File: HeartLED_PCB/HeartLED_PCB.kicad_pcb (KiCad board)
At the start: 2 copper layers, 58.8 x 52.2 mm, 37 parts, among them U1 ICM7555IBAZ-T, U2 CD4017BM96, U3 TPS61222DCKR, U4 HX SS12F44G4

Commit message: Routing done
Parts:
- removed BT1: Battery_Cell, Battery:BatteryHolder_Keystone_1060_1x2032
- removed C2, C3: 10uF, FOOTPRINTS:CL10A106MQ8NNNC
- removed the G*** at (123.5, 81.7)
- removed L1: 4.7uH, FOOTPRINTS:LQH3NPN4R7MMEL
- removed TP1, TP2, TP3: TestPoint, TestPoint:TestPoint_Pad_D1.0mm
- removed U3: TPS61222DCKR, FOOTPRINTS:TPS61222DCKR
- removed U4: HX SS12F44G4, FOOTPRINTS:HX SS12F44G4
- added G***: LOGO, FOOTPRINTS:raccoon, F.Cu at (128.5, 108.1)
- added SW1: SS12D00G3, FOOTPRINTS:SS12D00G3, F.Cu at (148.8, 93.9)
- C1: value 4.7uF -> 47uF; footprint FOOTPRINTS:CL10A475KP8NNNC -> Capacitor_THT:C_Radial_D5.0mm_H7.0mm_P2.00mm; moved to F.Cu
- H1: footprint MountingHole:MountingHole_2.1mm -> MountingHole:MountingHole_2.7mm
- R1: value 100k -> 1k; footprint FOOTPRINTS:0603WAJ0104T5E -> Resistor_THT:R_Axial_DIN0207_L6.3mm_D2.5mm_P7.62mm_Horizontal; moved to F.Cu
- R10, R3, R4, R5, R6, R7, R8, R9: value 3.3k -> 1k; footprint FOOTPRINTS:0402WGJ0332TCE -> Resistor_THT:R_Axial_DIN0207_L6.3mm_D2.5mm_P7.62mm_Horizontal
- R11: value 3.3k -> 10K; footprint FOOTPRINTS:0402WGJ0332TCE -> Resistor_THT:R_Axial_DIN0207_L6.3mm_D2.5mm_P7.62mm_Horizontal
- R12: value 3.3k -> 1OK; footprint FOOTPRINTS:0402WGJ0332TCE -> Resistor_THT:R_Axial_DIN0207_L6.3mm_D2.5mm_P7.62mm_Horizontal
- R2: value 10k -> 1k; footprint FOOTPRINTS:0402WGJ0103TCE -> Resistor_THT:R_Axial_DIN0207_L6.3mm_D2.5mm_P7.62mm_Horizontal; moved to F.Cu
- U1: value ICM7555IBAZ-T -> NE555DR; footprint FOOTPRINTS:ICM7555IBAZ-T -> FOOTPRINTS:NE555DR; moved to F.Cu
- U2: value CD4017BM96 -> 1066; footprint FOOTPRINTS:CD4017BM96 -> FOOTPRINTS:1066; moved to B.Cu
- moved R5 51.7 mm to (153.1, 102.0), turned to 180 degrees
- moved D4 51.3 mm to (156.8, 85.9), turned to 180 degrees
- moved D10 48.2 mm to (127.5, 121.4), turned to 0 degrees
- moved D6 46.9 mm to (113.8, 75.7)
- moved D7 42.5 mm to (102.2, 97.1), turned to 0 degrees
- moved R12 41.7 mm to (138.0, 116.4)
- moved R11 40.9 mm to (127.7, 116.4), turned to 180 degrees
- moved R4 39.8 mm to (150.4, 82.3)
- moved R8 35.5 mm to (140.0, 82.3)
- moved R2 34.9 mm to (106.9, 82.5)
- moved R1 29.8 mm to (124.9, 87.0)
- moved G*** 28.7 mm to (130.6, 112.3)
- moved D5 28.5 mm to (145.4, 108.5)
- moved R7 26.4 mm to (114.5, 87.0), turned to 180 degrees
- moved R9 26.3 mm to (142.8, 87.0), turned to 0 degrees
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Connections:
- C1 pad 1: Net-(U1-THRESHOLD) -> Net-(U1-THRES)
- D1 pad 2: Net-(D1-A) -> VCC
- D10 pad 1: Net-(D10-K) -> GND
- D2 pad 2: Net-(D2-A) -> VCC
- D3 pad 2: Net-(D3-A) -> VCC
- D4 pad 2: Net-(D4-A) -> VCC
- D5 pad 2: Net-(D5-A) -> VCC
- D6 pad 1: Net-(D6-K) -> GND
- D7 pad 1: Net-(D7-K) -> GND
- D8 pad 1: Net-(D8-K) -> GND
- D9 pad 1: Net-(D9-K) -> GND
- R1 pad 1: ASTABLE_OUTPUT -> Net-(D1-K)
- R1 pad 2: Net-(U1-THRESHOLD) -> Net-(U1-OUT)
- R10 pad 1: GND -> Net-(U1-OUT)
- R10 pad 2: Net-(D8-K) -> Net-(D10-A)
- R11 pad 1: GND -> Net-(U1-DISCH)
- R11 pad 2: Net-(D9-K) -> Net-(U1-THRES)
- R12 pad 1: GND -> VCC
- R12 pad 2: Net-(D10-K) -> Net-(U1-DISCH)
- R2 pad 1: Net-(U1-DISCHARGE) -> Net-(D2-K)
- R2 pad 2: +5V -> Net-(U1-OUT)
- R3 pad 1: Net-(D1-K) -> Net-(D3-K)
- R3 pad 2: GND -> Net-(U1-OUT)
- R4 pad 1: Net-(D2-K) -> Net-(D4-K)
- R4 pad 2: GND -> Net-(U1-OUT)
- R5 pad 1: Net-(D3-K) -> Net-(D5-K)
- R5 pad 2: GND -> Net-(U1-OUT)
- R6 pad 1: Net-(D4-K) -> Net-(U1-OUT)
- R6 pad 2: GND -> Net-(D6-A)
- R7 pad 1: GND -> Net-(U1-OUT)
- R7 pad 2: Net-(D5-K) -> Net-(D7-A)
- R8 pad 1: Net-(D6-K) -> Net-(U1-OUT)
- R8 pad 2: GND -> Net-(D8-A)
- R9 pad 1: Net-(D7-K) -> Net-(U1-OUT)
- R9 pad 2: GND -> Net-(D9-A)
- U1 pad 2: Net-(U1-THRESHOLD) -> Net-(U1-THRES)
- U1 pad 3: ASTABLE_OUTPUT -> Net-(U1-OUT)
- U1 pad 4: +5V -> VCC
- U1 pad 5: GND -> unconnected-(U1-CONT-Pad5)
- U1 pad 6: Net-(U1-THRESHOLD) -> Net-(U1-THRES)
- U1 pad 7: Net-(U1-DISCHARGE) -> Net-(U1-DISCH)
- U1 pad 8: +5V -> VCC
- U2 pad 1: Net-(D1-A) -> GND
- U2 pad 2: Net-(D2-A) -> Net-(SW1-Pad2)
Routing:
- net Net-(U1-OUT): track 0.00 -> 104.6 mm
- net +5V: track 69.5 -> 0.00 mm, vias 1 -> 0
- net +3V: track 49.1 -> 0.00 mm
- net Net-(U1-THRES): track 0.00 -> 38.9 mm
- net ASTABLE_OUTPUT: track 36.8 -> 0.00 mm, vias 1 -> 0
- net Net-(D3-A): track 27.3 -> 0.00 mm
- net Net-(D2-A): track 25.8 -> 0.00 mm
- net Net-(U1-THRESHOLD): track 25.1 -> 0.00 mm
- net Net-(U1-DISCH): track 0.00 -> 23.4 mm
- net Net-(BT1-+): track 20.2 -> 0.00 mm
- net Net-(D4-A): track 18.2 -> 0.00 mm
- net Net-(D9-A): track 29.0 -> 11.0 mm
- net Net-(SW1-Pad2): track 0.00 -> 16.9 mm
- net Net-(D5-A): track 12.3 -> 0.00 mm
- net Net-(D1-A): track 10.4 -> 0.00 mm
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- added copper zone on F.Cu, net VCC
- removed copper zone on F.Cu, net GND
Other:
- board size 58.8 x 52.2 mm -> 61.9 x 55.1 mm
- board text removed: "Happy Valentine's Day ( ˘ ³˘)♥"
- board text removed: "github.com/ fectec/ HeartLED"
- board text removed: "v1.0.0"
- board text removed: "© 2025"

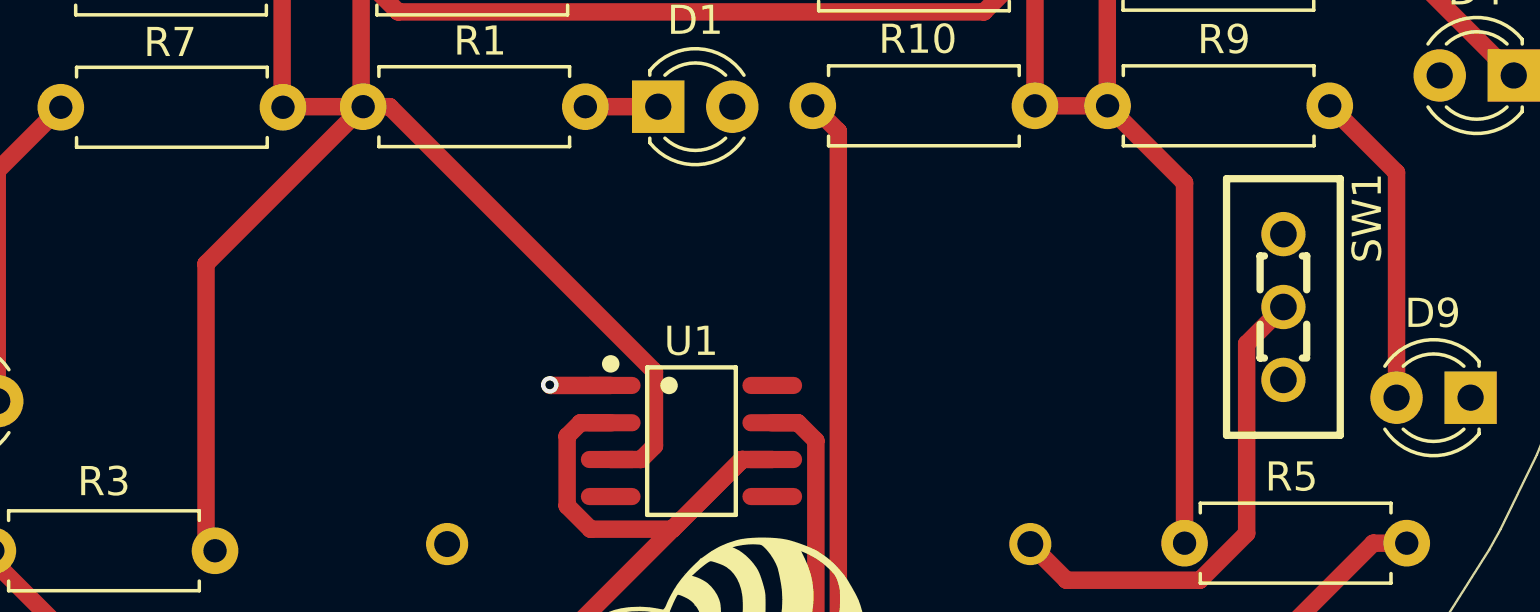
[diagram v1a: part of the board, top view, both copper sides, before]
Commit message: Added silkscreen logos
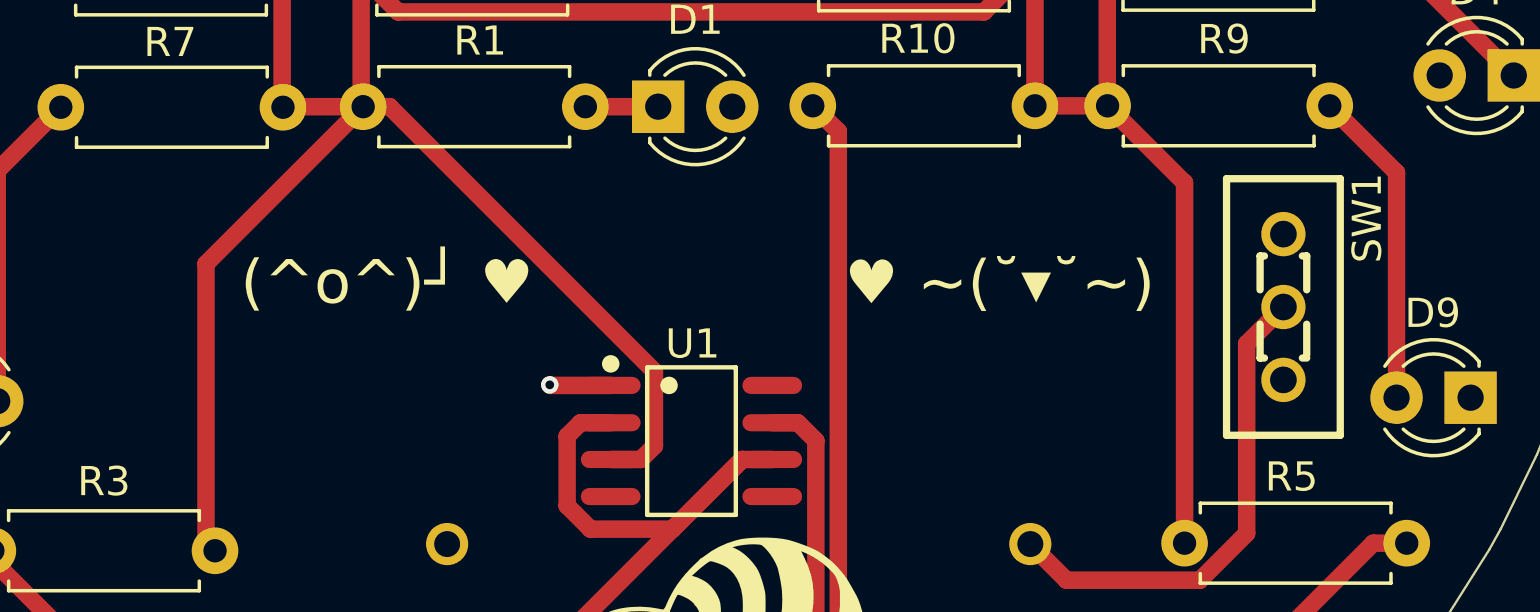
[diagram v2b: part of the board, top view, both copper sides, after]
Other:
- board text added: "(^o^)┘ ♥"
- board text added: "♥ ~(˘▾˘~)"

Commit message: Cleanup
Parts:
- added J1: Conn_01x02_Pin, Connector_PinHeader_2.54mm:PinHeader_1x02_P2.54mm_Vertical, F.Cu at (108.0, 92.5)
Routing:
- net Net-(U1-OUT): track 104.6 -> 104.1 mm
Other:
- board text added: "Happy Valentine's Day!"
- board text added: "github.com/ fectec/ HeartLED"
